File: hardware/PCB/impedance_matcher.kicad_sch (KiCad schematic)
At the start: 44 parts, among them Q1 PC817, U1 TLV2372IP

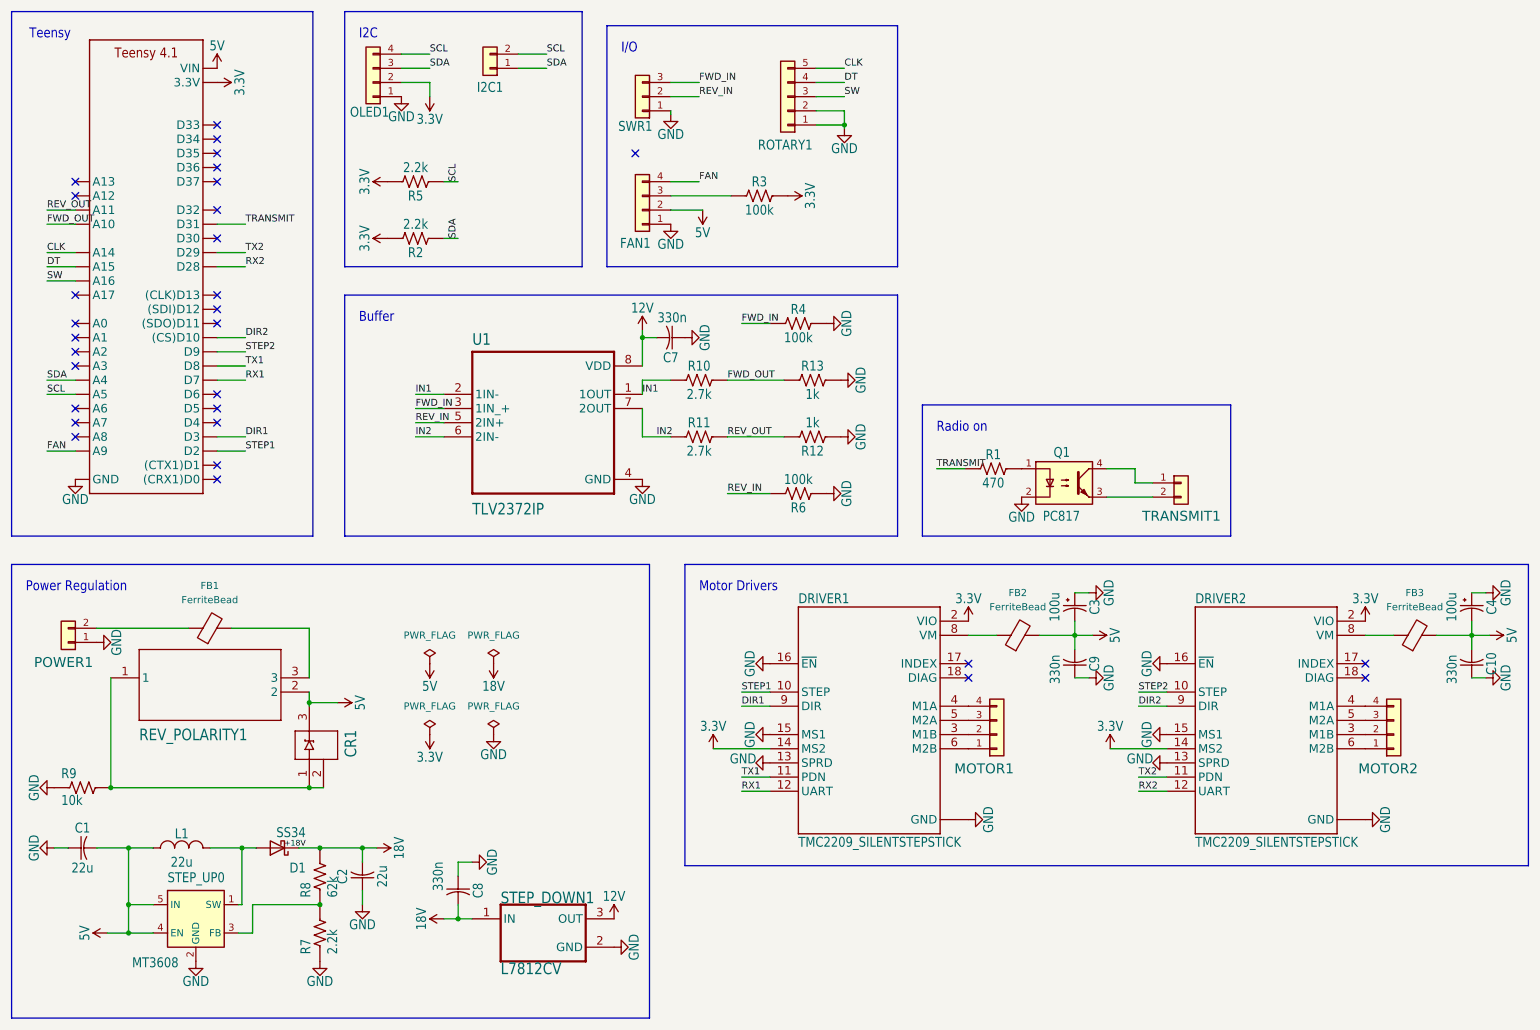
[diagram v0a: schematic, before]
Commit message: Clean up nets and layers
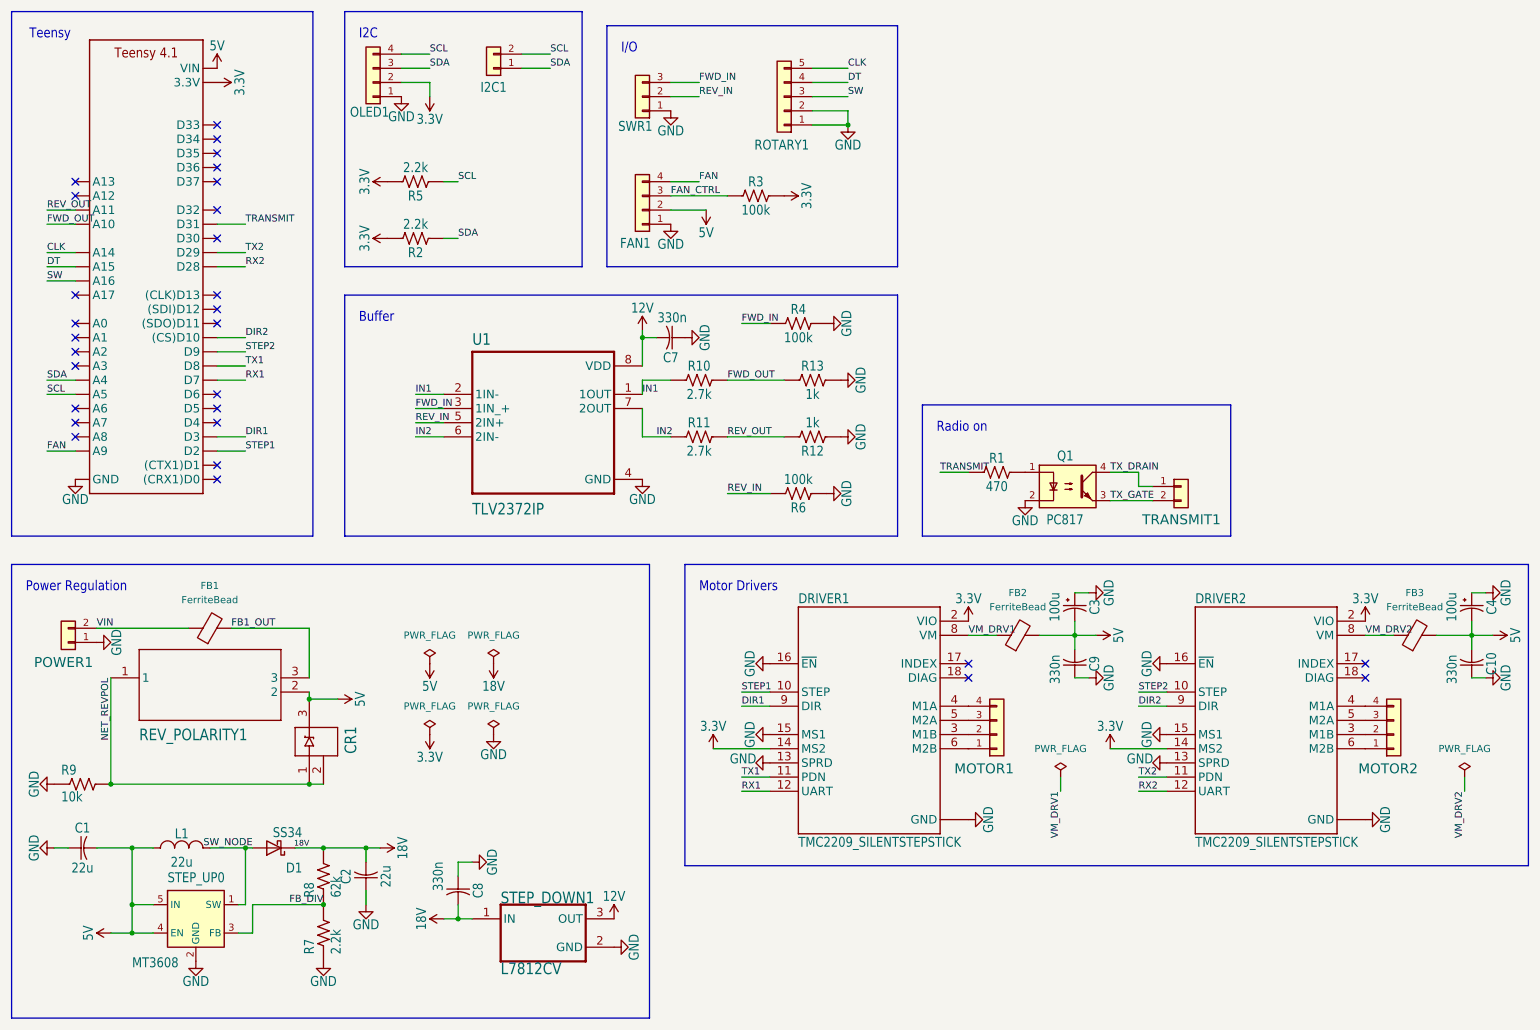
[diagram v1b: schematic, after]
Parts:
- C1, C2: MPN (none) -> CL21A226MAQNNNE; Manufacturer (none) -> Samsung Electro-Mechanics
- C10, C7, C8, C9: MPN (none) -> 0805B334K500NT; Manufacturer (none) -> FH (Guangdong Fenghua)
- CR1: MPN (none) -> BZX84C5V6
- D1: MPN (none) -> SS34
- FB1, FB2, FB3: MPN (none) -> MPZ2012S101AT000; Manufacturer (none) -> TDK
- L1: MPN (none) -> SMNR5040-220MT; Manufacturer (none) -> Sunlord
- Q1: MPN (none) -> PC817B
- R1: MPN (none) -> 0805W8F4700T5E; Manufacturer (none) -> UNI-ROYAL(Uniroyal Elec)
- R10, R11: MPN (none) -> 0805W8F2701T5E; Manufacturer (none) -> UNI-ROYAL(Uniroyal Elec)
- R12, R13: MPN (none) -> 0805W8F1001T5E; Manufacturer (none) -> UNI-ROYAL(Uniroyal Elec)
- R2, R5, R7: MPN (none) -> 0805W8F2201T5E; Manufacturer (none) -> UNI-ROYAL(Uniroyal Elec)
- R3, R4, R6: MPN (none) -> 0805W8F1003T5E; Manufacturer (none) -> UNI-ROYAL(Uniroyal Elec)
- R8: MPN (none) -> 0805W8F6202T5E; Manufacturer (none) -> UNI-ROYAL(Uniroyal Elec)
- R9: MPN (none) -> 0805W8F1002T5E; Manufacturer (none) -> UNI-ROYAL(Uniroyal Elec)
- REV_POLARITY1: MPN (none) -> DMP6180SK3-13; Manufacturer (none) -> Diodes Incorporated
- STEP_DOWN1: MPN (none) -> L7812CV; Manufacturer (none) -> STMicroelectronics
- STEP_UP0: MPN (none) -> MT3608; Manufacturer (none) -> XLSEMI
- U1: LCSC Part (none) -> C2878991; MPN (none) -> TLV2372IP; Manufacturer (none) -> Texas Instruments
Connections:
- net VIN: now reaches FB1.1, POWER1.2 (Pin_2)
- net TX_DRAIN: now reaches Q1.4, TRANSMIT1.1 (Pin_1)
- net TX_GATE: now reaches Q1.3, TRANSMIT1.2 (Pin_2)
- net SW_NODE: now reaches D1.2 (A), L1.2, STEP_UP0.1 (SW)
- net FB_DIV: now reaches R7.2, R8.1, STEP_UP0.3 (FB)
- net NET_REVPOL: now reaches CR1.1, CR1.2, R9.2, REV_POLARITY1.1
- net FB1_OUT: now reaches FB1.2, REV_POLARITY1.3
- net VM_DRV1: now reaches DRIVER1.8 (VM), FB2.1
- net VM_DRV2: now reaches DRIVER2.8 (VM), FB3.1
- net FAN_CTRL: now reaches FAN1.3 (Pin_3), R3.1
- no-connect marks 30 -> 29
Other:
- moved on the sheet: C2, CR1, D1, I2C1, Q1, R1, R3, R7, R8, R9, ROTARY1, TRANSMIT1

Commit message: SWR input protection
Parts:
- added D2: BAV99S, Package_TO_SOT_SMD:SOT-363_SC-70-6, symbol Diode:BAV99S
- added R14, R15: 1k, Resistor:RESC2012X65, symbol Resistor:R-USCHIP-1206(3216-METRIC)
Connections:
- net 12V: now also D2.2 (K2), D2.5 (K4)
- net FWD_IN: now also R14.1; no longer U1.3 (1IN_+)
- net GND: now also D2.1 (A1), D2.4 (A3)
- net REV_IN: now also R15.1; no longer U1.5 (2IN+)
- new net FWD_BUF: D2.6 (K3A4), R14.2, U1.3 (1IN_+)
- new net REV_BUF: D2.3 (K1A2), R15.2, U1.5 (2IN+)
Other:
- moved on the sheet: Q1, R1, TRANSMIT1

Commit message: change i2c1, rotary1, oled1, fan1, swr1 to JST PH 2.0mm and update C3/C4 pad1 to be 5V instead of pad2
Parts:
- FAN1, OLED1: footprint Project Connectors:B4B-XH-A -> Connector_JST:JST_PH_B4B-PH-K_1x04_P2.00mm_Vertical
- I2C1: footprint Project Connectors:B2B-XH-A -> Connector_JST:JST_PH_B2B-PH-K_1x02_P2.00mm_Vertical
- ROTARY1: footprint B5B-XH-A:JST_B5B-XH-A -> Connector_JST:JST_PH_B5B-PH-K_1x05_P2.00mm_Vertical
- SWR1: footprint Project Connectors:B3B-XH-A -> Connector_JST:JST_PH_B3B-PH-K_1x03_P2.00mm_Vertical
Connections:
- net 5V: now also C3.1 (+), C4.1 (+); no longer C3.2 (-), C4.2 (-)
- net GND: now also C3.2 (-), C4.2 (-); no longer C3.1 (+), C4.1 (+)
- net SCL: now also I2C1.1 (Pin_1); no longer I2C1.2 (Pin_2)
- net SDA: now also I2C1.2 (Pin_2); no longer I2C1.1 (Pin_1)
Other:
- moved on the sheet: C3, C4
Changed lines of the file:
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@@
 		)
 	)
-	(label "SCL"
+	(label "SDA"
 		(at 116.84 25.4 0)
 		(effects
@@
 		)
 	)
-	(label "SDA"
+	(label "SCL"
 		(at 116.84 27.94 0)
 		(effects
@@
 			)
 		)
-		(property "Footprint" "Project Connectors:B3B-XH-A"
+		(property "Footprint" "Connector_JST:JST_PH_B3B-PH-K_1x03_P2.00mm_Vertical"
 			(at 133.35 33.02 0)
 			(hide yes)
@@
 	(symbol
 		(lib_id "Capacitor:C-POL-USRADIAL-11MM-DIA")
-		(at 281.94 124.46 270)
+		(at 281.94 124.46 90)
 		(unit 1)
 		(body_style 1)
@@
 			)
 		)
-		(property "Footprint" "B5B-XH-A:JST_B5B-XH-A"
+		(property "Footprint" "Connector_JST:JST_PH_B5B-PH-K_1x05_P2.00mm_Vertical"
 			(at 158.75 33.02 0)
 			(hide yes)
@@
 			)
 		)
-		(property "Footprint" "Project Connectors:B4B-XH-A"
+		(property "Footprint" "Connector_JST:JST_PH_B4B-PH-K_1x04_P2.00mm_Vertical"
 			(at 85.09 30.48 0)
 			(hide yes)
@@
 			)
 		)
-		(property "Footprint" "Project Connectors:B4B-XH-A"
+		(property "Footprint" "Connector_JST:JST_PH_B4B-PH-K_1x04_P2.00mm_Vertical"
 			(at 133.35 53.34 0)
 			(hide yes)
@@
 			)
 		)
-		(property "Footprint" "Project Connectors:B2B-XH-A"
+		(property "Footprint" "Connector_JST:JST_PH_B2B-PH-K_1x02_P2.00mm_Vertical"
 			(at 106.68 27.94 0)
 			(hide yes)
@@
 	(symbol
 		(lib_id "Capacitor:C-POL-USRADIAL-11MM-DIA")
-		(at 210.82 124.46 270)
+		(at 210.82 124.46 90)
 		(unit 1)
 		(body_style 1)

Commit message: Correct driver UART, detector loading, and fan interface
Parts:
- added C11, C12, C13, C14: 100n, Capacitor:CAPC2012X110, symbol Capacitor:C-USCHIP-0805(2012-METRIC)
- added R16: 2.2k, Resistor_SMD:R_0805_2012Metric, symbol Resistor:R-USCHIP-0805(2012-METRIC)
- added R17: 100k, Resistor:RESC2012X65, symbol Resistor:R-USCHIP-0805(2012-METRIC)
- added R18, R19: 1k, Resistor:RESC2012X65, symbol Resistor:R-USCHIP-0805(2012-METRIC)
- added U2: SN74AHCT1G14, Logic:SOT-23-5, symbol Logic:SN74AHCT1G14DBV
- A1: MPN (none) -> TEENSY41; Manufacturer (none) -> PJRC
- C3, C4: footprint Capacitor:CAPPRD508W65D1000H1100B -> Capacitor:CP_Radial_D5.0mm_P5.08mm_Formed; MPN (none) -> EEU-FR1C101B; Manufacturer (none) -> Panasonic
- D2: value BAV99S -> BAV199S-Q; symbol Diode:BAV99S -> Diode:BAV199S-Q; LCSC Part (none) -> C7507590; MPN (none) -> BAV199S-QZ; Manufacturer (none) -> Nexperia
- DRIVER1, DRIVER2: value TMC2209_SILENTSTEPSTICK -> BTT_TMC2209_V1.3; MPN (none) -> TMC2209 V1.3; Manufacturer (none) -> BIGTREETECH
- FAN1, MOTOR1, MOTOR2, OLED1: MPN (none) -> B4B-PH-K-S; Manufacturer (none) -> JST
- I2C1: MPN (none) -> B2B-PH-K-S; Manufacturer (none) -> JST
- POWER1, TRANSMIT1: MPN (none) -> PRT-10571; Manufacturer (none) -> SparkFun
- R10, R11: value 2.7k -> 3.3k; LCSC Part C17530 -> C26010; MPN 0805W8F2701T5E -> 0805W8F3301T5E
- R4, R6: value 100k -> 100M; LCSC Part C149504 -> C137480; MPN 0805W8F1003T5E -> RC0805JR-07100ML; Manufacturer UNI-ROYAL(Uniroyal Elec) -> YAGEO
- ROTARY1: MPN (none) -> B5B-PH-K-S; Manufacturer (none) -> JST
- SWR1: MPN (none) -> B3B-PH-K-S; Manufacturer (none) -> JST
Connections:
- net 12V: now also C11.2, R16.2
- net 5V: now also C14.2, U2.5 (VCC); no longer C10.2, C3.1 (+), C4.1 (+), C9.2
- net FAN: now also R17.1, U2.2; no longer FAN1.4 (Pin_4)
- net FWD_OUT: now also C12.2
- net GND: now also DRIVER1.11 (CLK), DRIVER2.11 (CLK), C11.1, C12.1, C13.1, C14.1, R16.1, R17.2, U2.3 (GND); no longer DRIVER1.13 (SPRD), DRIVER2.13 (SPRD)
- net REV_OUT: now also C13.2
- net RX1: now also DRIVER1.13 (PDN_UART), R18.2; no longer DRIVER1.12 (UART)
- net RX2: now also DRIVER2.13 (PDN_UART), R19.2; no longer DRIVER2.12 (UART)
- net TX1: now also R18.1; no longer DRIVER1.11 (PDN)
- net TX2: now also R19.1; no longer DRIVER2.11 (PDN)
- net VM_DRV1: now also C3.1 (+), C9.2
- net VM_DRV2: now also C10.2, C4.1 (+)
- net FAN_CTRL renamed FAN_TACH
- new net FAN_PWM: FAN1.4 (Pin_4), U2.4
- no-connect marks 29 -> 32
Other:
- note added: "ASSEMBLY: cut Teensy VIN-VUSB link before using external 5 V + USB. Verify VIN-to-VUSB isolation before connecting the computer."
- note added: "BTT V1.3 UART: R18/R19 = 1k TX isolation. RX to PDN_UART; alternate TX header NC. MS1=LOW / MS2=HIGH: 64 steps, UART address 2. Standalone: UART GPIOs INPUT. Power-cycle after UART. Leave legacy auxiliary holes 17/18 empty."
- note added: "LOW = full speed PWM: inverted, 25 kHz"
- note added: "Local bypass and ADC filters C12/C13: nominal pole 2.07 kHz"
